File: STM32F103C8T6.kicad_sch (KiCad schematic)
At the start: 55 parts, among them J1 USB_Device, J2 USB_TTL, P1 L-Pin, P2 R-Pin, P3 DEBUG, P4 POWER-R, P5 POWER-L, SW1 NRST, U1 MIC5219-3.3YM5, U2 CH340E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

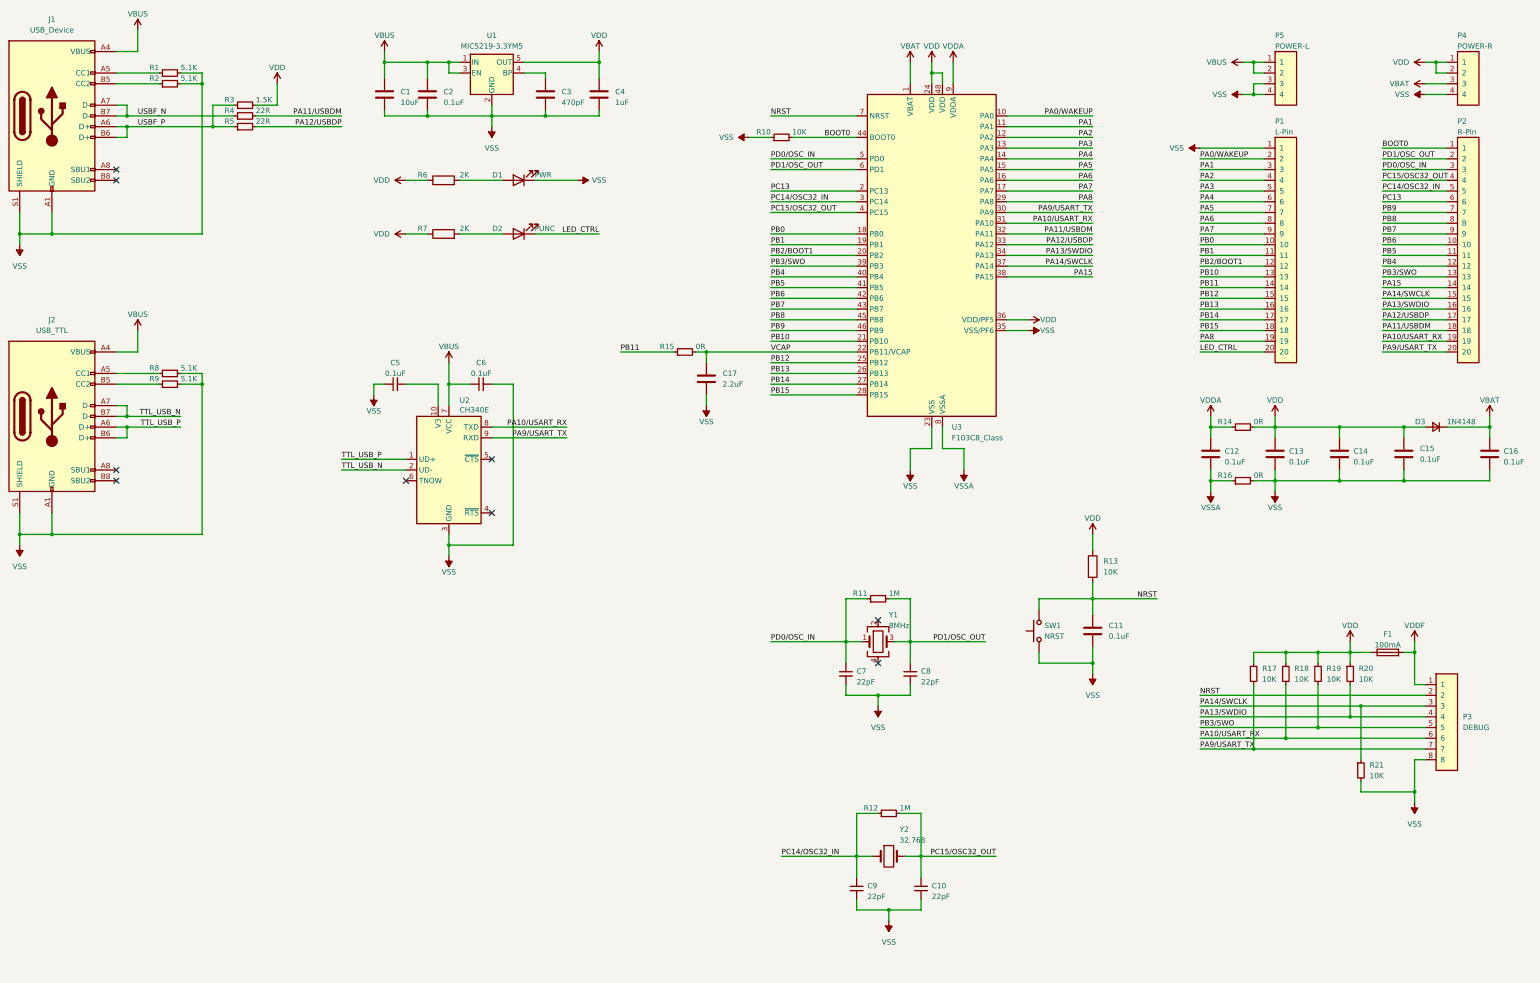
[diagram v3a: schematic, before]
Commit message: 更新引脚链接，增加晶振引脚的跳接焊盘
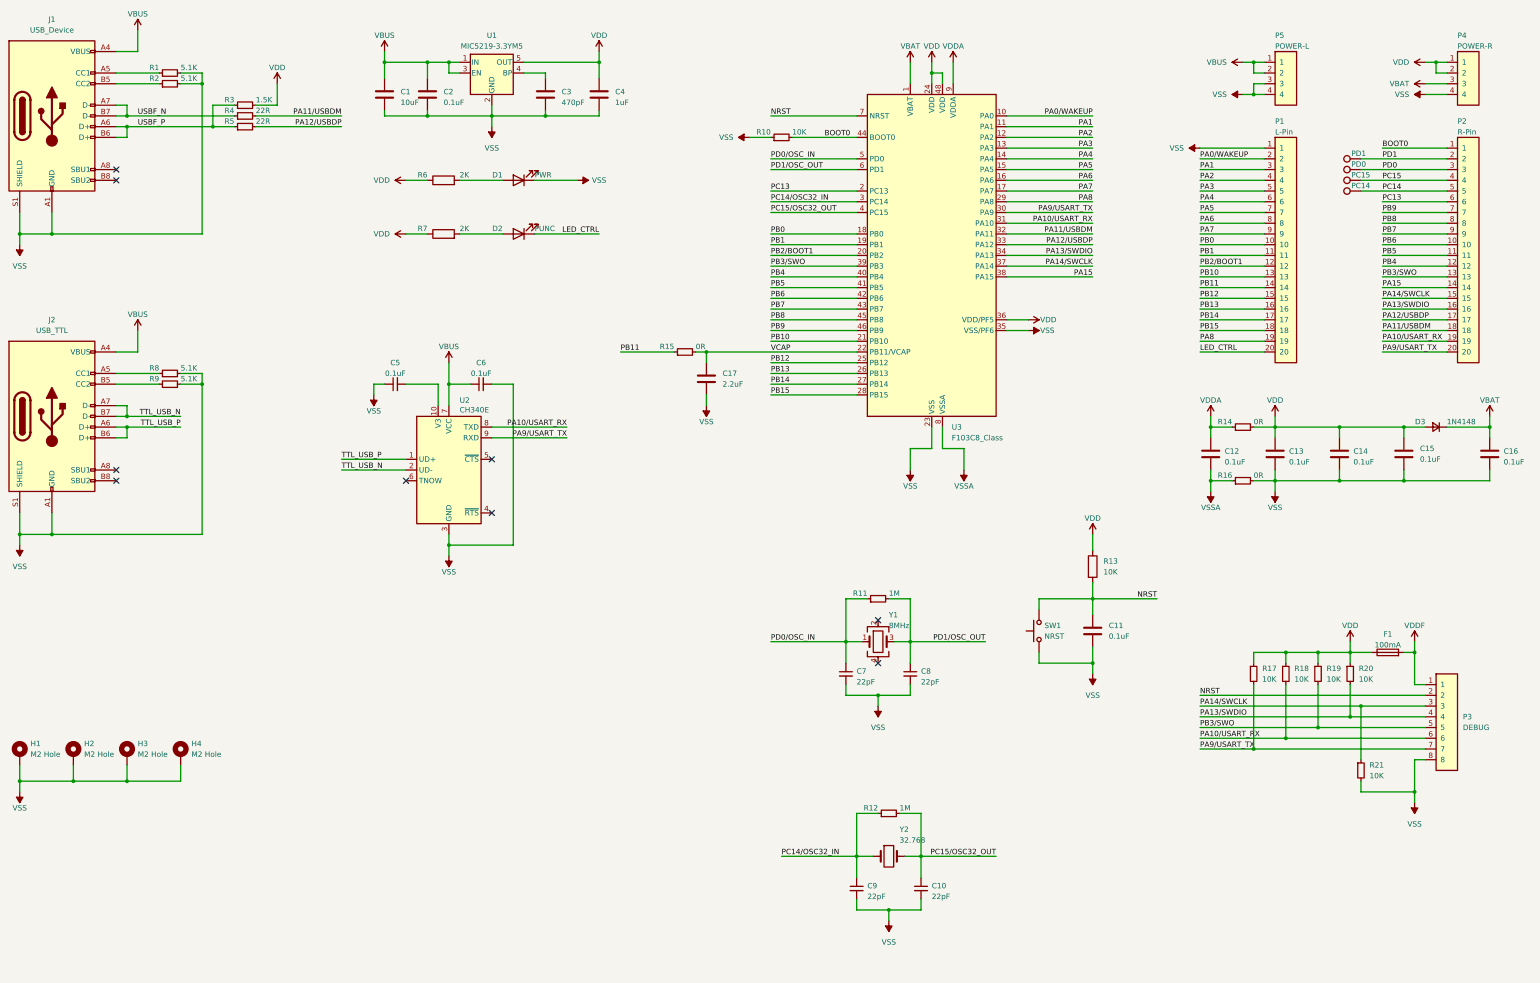
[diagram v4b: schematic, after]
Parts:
- added H1, H2, H3, H4: M2 Hole, Append_Connector:Hole_2×4.5mm, symbol Mechanical:MountingHole_Pad_MP
- added TP1: PD1, Append_Connector:PAD_Semicircular_1mm, symbol Connector:TestPoint
- added TP2: PD0, Append_Connector:PAD_Semicircular_1mm, symbol Connector:TestPoint
- added TP3: PC15, Append_Connector:PAD_Semicircular_1mm, symbol Connector:TestPoint
- added TP4: PC14, Append_Connector:PAD_Semicircular_1mm, symbol Connector:TestPoint
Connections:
- net PC14/OSC32_IN: no longer P2.5
- net PC15/OSC32_OUT: no longer P2.4
- net PD0/OSC_IN: no longer P2.3
- net PD1/OSC_OUT: no longer P2.2
- net VSS: now also H1.MP, H2.MP, H3.MP, H4.MP
- new net PC14: P2.5, TP4.1
- new net PC15: P2.4, TP3.1
- new net PD0: P2.3, TP2.1
- new net PD1: P2.2, TP1.1

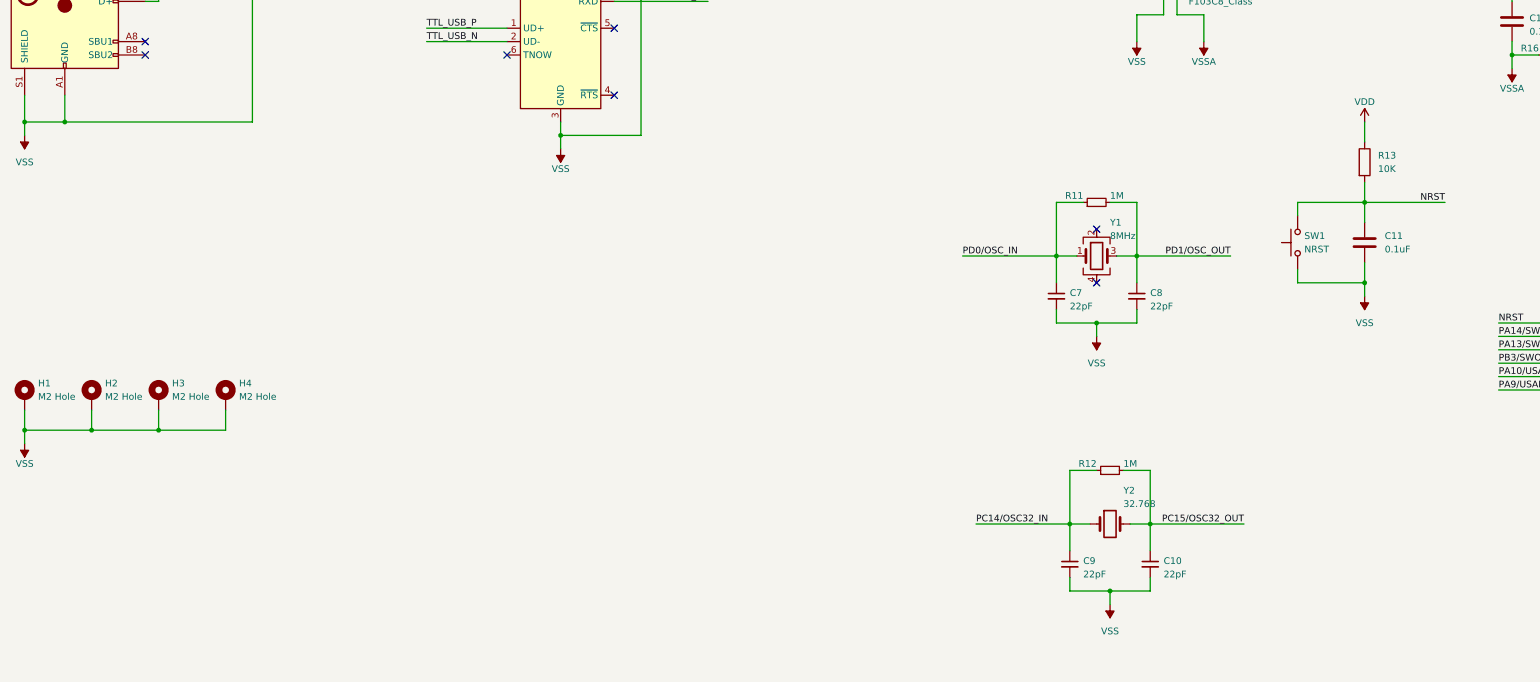
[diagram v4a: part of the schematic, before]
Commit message: 优化电源走线
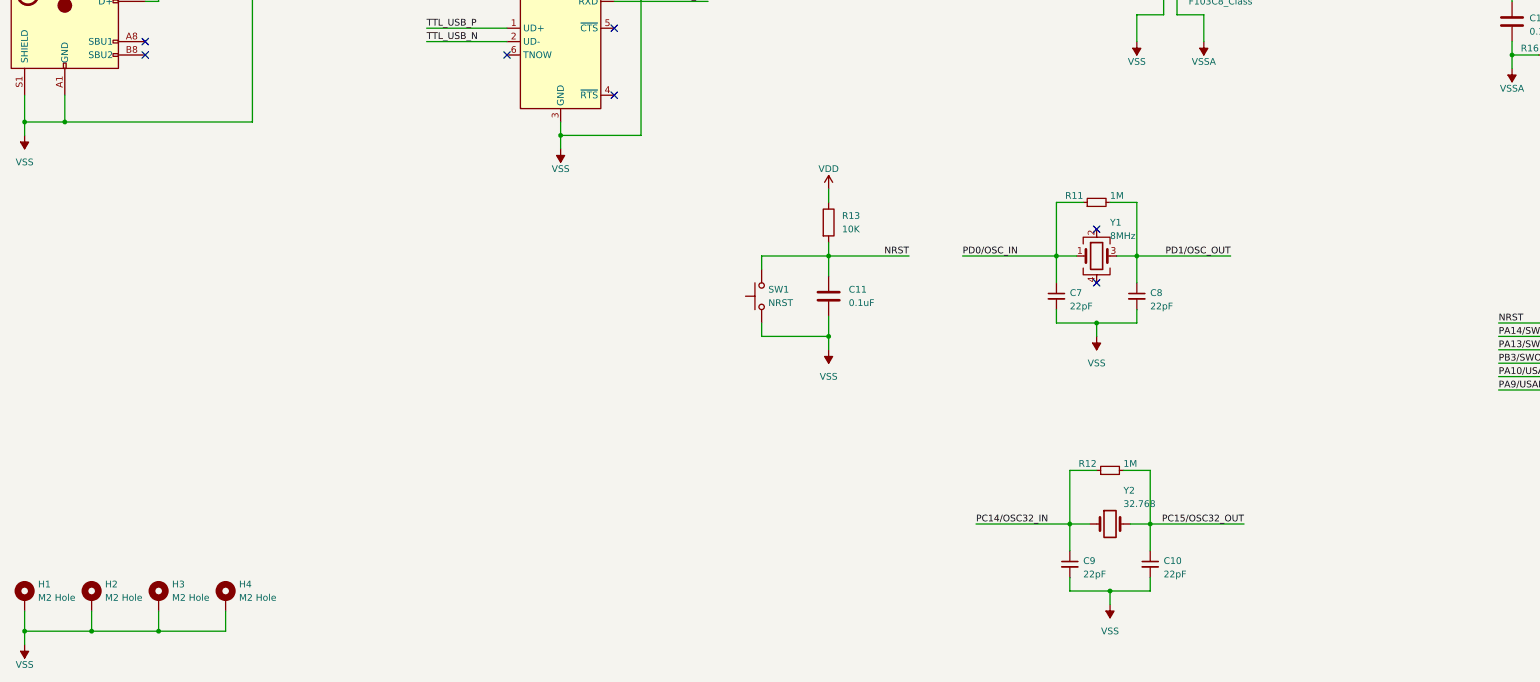
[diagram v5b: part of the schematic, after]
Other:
- moved on the sheet: C11, H1, H2, H3, H4, R13, SW1
